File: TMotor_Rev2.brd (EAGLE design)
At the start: 56.5 x 79 mm, 29 parts, among them U1 INA125U, U2 INA125U

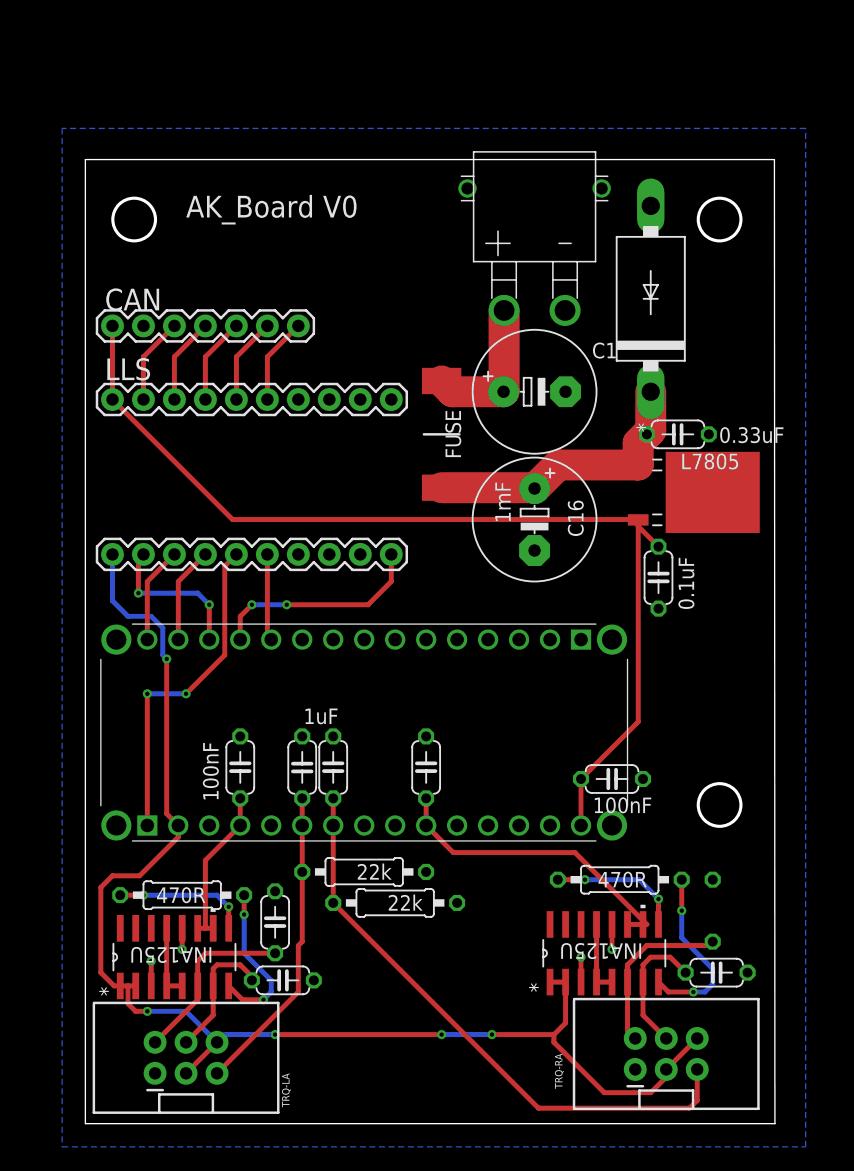
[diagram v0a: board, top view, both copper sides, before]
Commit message: Added integrated PCB version w/ MCP25625
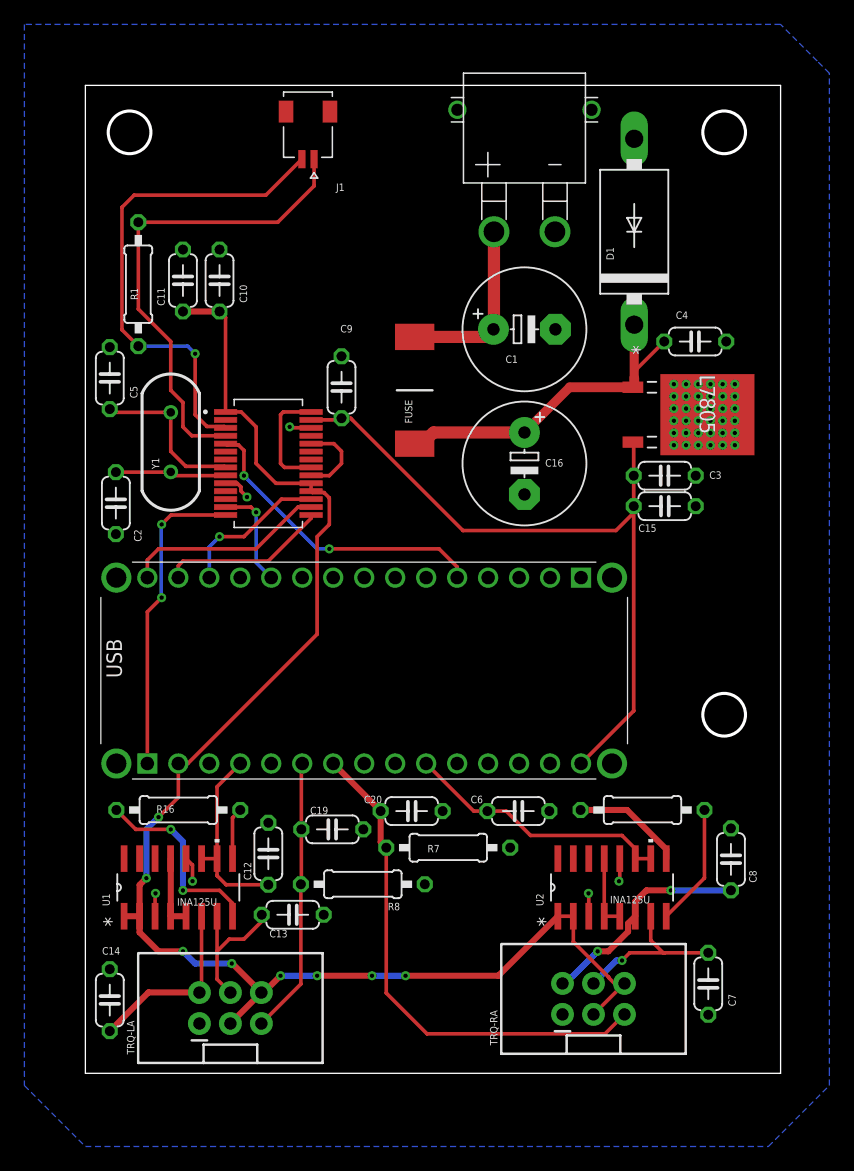
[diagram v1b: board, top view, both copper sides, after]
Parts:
- removed J2: (no value), SparkFun-Connectors:1X10
- removed J3: (no value), SparkFun-Connectors:1X07
- added C10, C11, C9: 0.1uF, rcl:C050-024X044
- added C2, C5: 22pF, rcl:C050-024X044
- added R1: 120Ω, rcl:0207/10
- added U3: MCP25625-E/SS, MCP25625-E_SS:SOP65P780X200-28N
- added Y1: 16MHz, SnapEDA-Library_Paul:IQD-HC-49-4H
- J1: value (none) -> 5015680207; device SparkFun-Connectors:1X10 -> SnapEDA-Library_Paul:MOLEX_5015680207
- moved J1 38.5 mm to (18.2, 77.5), turned to 180 degrees
- moved C15 22.8 mm to (47.5, 46.5)
- moved C14 15.0 mm to (2.00, 6.00)
- moved C3 8.38 mm to (47.5, 49.0), turned to 180 degrees
- moved C6 8.37 mm to (35.5, 21.5), turned to 0 degrees
- moved C4 7.74 mm to (50.0, 60.0)
- moved TRQ-RA 7.48 mm to (41.7, 6.10)
- moved C12 7.45 mm to (15.0, 18.0)
- moved C20 7.36 mm to (26.8, 21.5), turned to 0 degrees
- moved R16 6.99 mm to (7.62, 21.6), turned to 0 degrees
- moved U$9 6.51 mm to (36.0, 69.0)
- moved L7805 6.39 mm to (51.0, 54.0)
- moved R7 6.28 mm to (29.8, 18.5)
- moved R14 6.01 mm to (45.7, 21.6)
- moved U1 5.72 mm to (7.62, 15.2)
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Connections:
- removed net H_CS: J2.9, J3.3
- removed net H_INT: J2.5, J3.7
- removed net H_MISO: J2.8, J3.4
- removed net H_MOSI: J2.7, J3.5
- removed net H_SCK: J2.6, J3.6
- removed net N$27: J1.7
- removed net N$28: J1.8
- removed net N$29: J1.9
- new net CANH-: J1.1, R1.2, U3.4
- new net CANL-: J1.2, R1.1, U3.3
- new net D2: U3.5, USB.B5
- new net N$1: C2.1, U3.9, Y1.2
- new net N$2: C5.1, U3.8, Y1.1
- new net RXD: U3.21, U3.28
- new net TXD: U3.20, U3.24
- net 3.3V: now also C10.1, C11.1, U3.1, U3.18, U3.19; no longer J1.1
- net CAN_CS: now also U3.17; no longer J1.2
- net CAN_INT: now also U3.13; no longer J1.6
- net GND: now also C10.2, C11.2, C2.2, C5.2, C9.2, U3.10, U3.26; no longer J2.1, J3.2
- net LLS_OE: no longer J1.10
- net MISO: now also U3.16; no longer J1.3
- net MOSI: now also U3.15; no longer J1.4
- net SCK: now also U3.14; no longer J1.5
- net VIN: now also C9.1, U3.27; no longer J2.10, J3.1
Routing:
- net CANL-: track 0.00 -> 41.2 mm, vias 0 -> 1
- net CANH-: track 0.00 -> 39.9 mm
- net D2: track 0.00 -> 25.3 mm, vias 0 -> 2
- net VIN: track 83.1 -> 59.6 mm
- net LLS_OE: track 17.7 -> 0.00 mm, vias 2 -> 0
- net 3.3V: track 108.7 -> 123.7 mm, vias 5 -> 8
- net N$2: track 0.00 -> 13.3 mm
- net RXD: track 0.00 -> 9.24 mm
- net N$1: track 0.00 -> 9.14 mm
- net MISO: track 7.91 -> 16.7 mm
- net GND: track 7.86 -> 15.0 mm, vias 4 -> 42
- net H_MOSI: track 7.08 -> 0.00 mm
- net H_SCK: track 7.08 -> 0.00 mm
- net H_MISO: track 7.08 -> 0.00 mm
- net H_INT: track 7.08 -> 0.00 mm
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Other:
- board size 56.5 x 79 mm -> 57 x 81 mm
- board text removed: "AK_Board V0"
- board text removed: "CAN"
- board text removed: "LLS"
